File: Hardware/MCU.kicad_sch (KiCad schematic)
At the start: 32 parts, among them SW3 MCU_BOOT, SW4 reset, U14 STM32H743VITx, Y3 8MHz 12pF

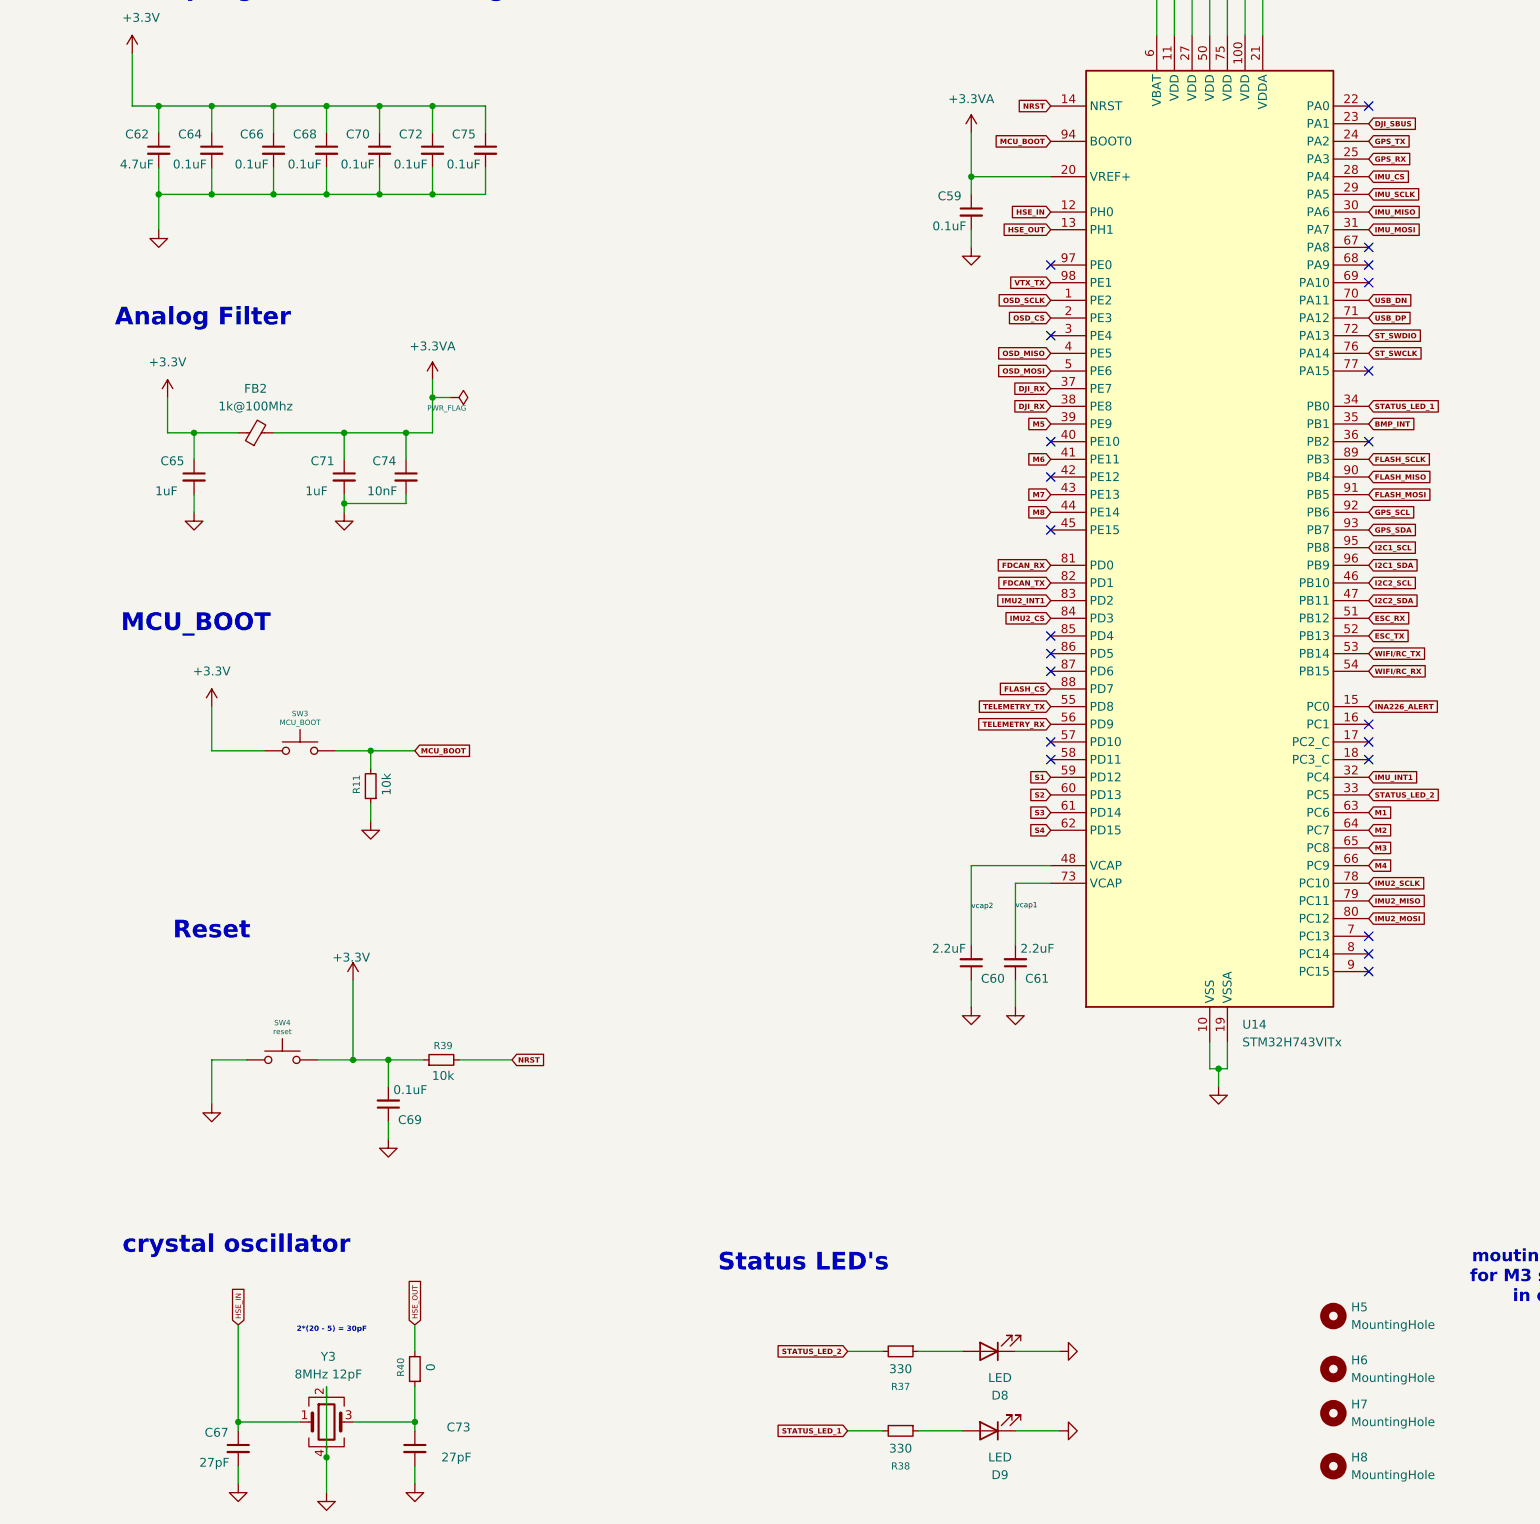
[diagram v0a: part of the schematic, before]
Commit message: Added Necessary Connectors, pads and comments in the respective file
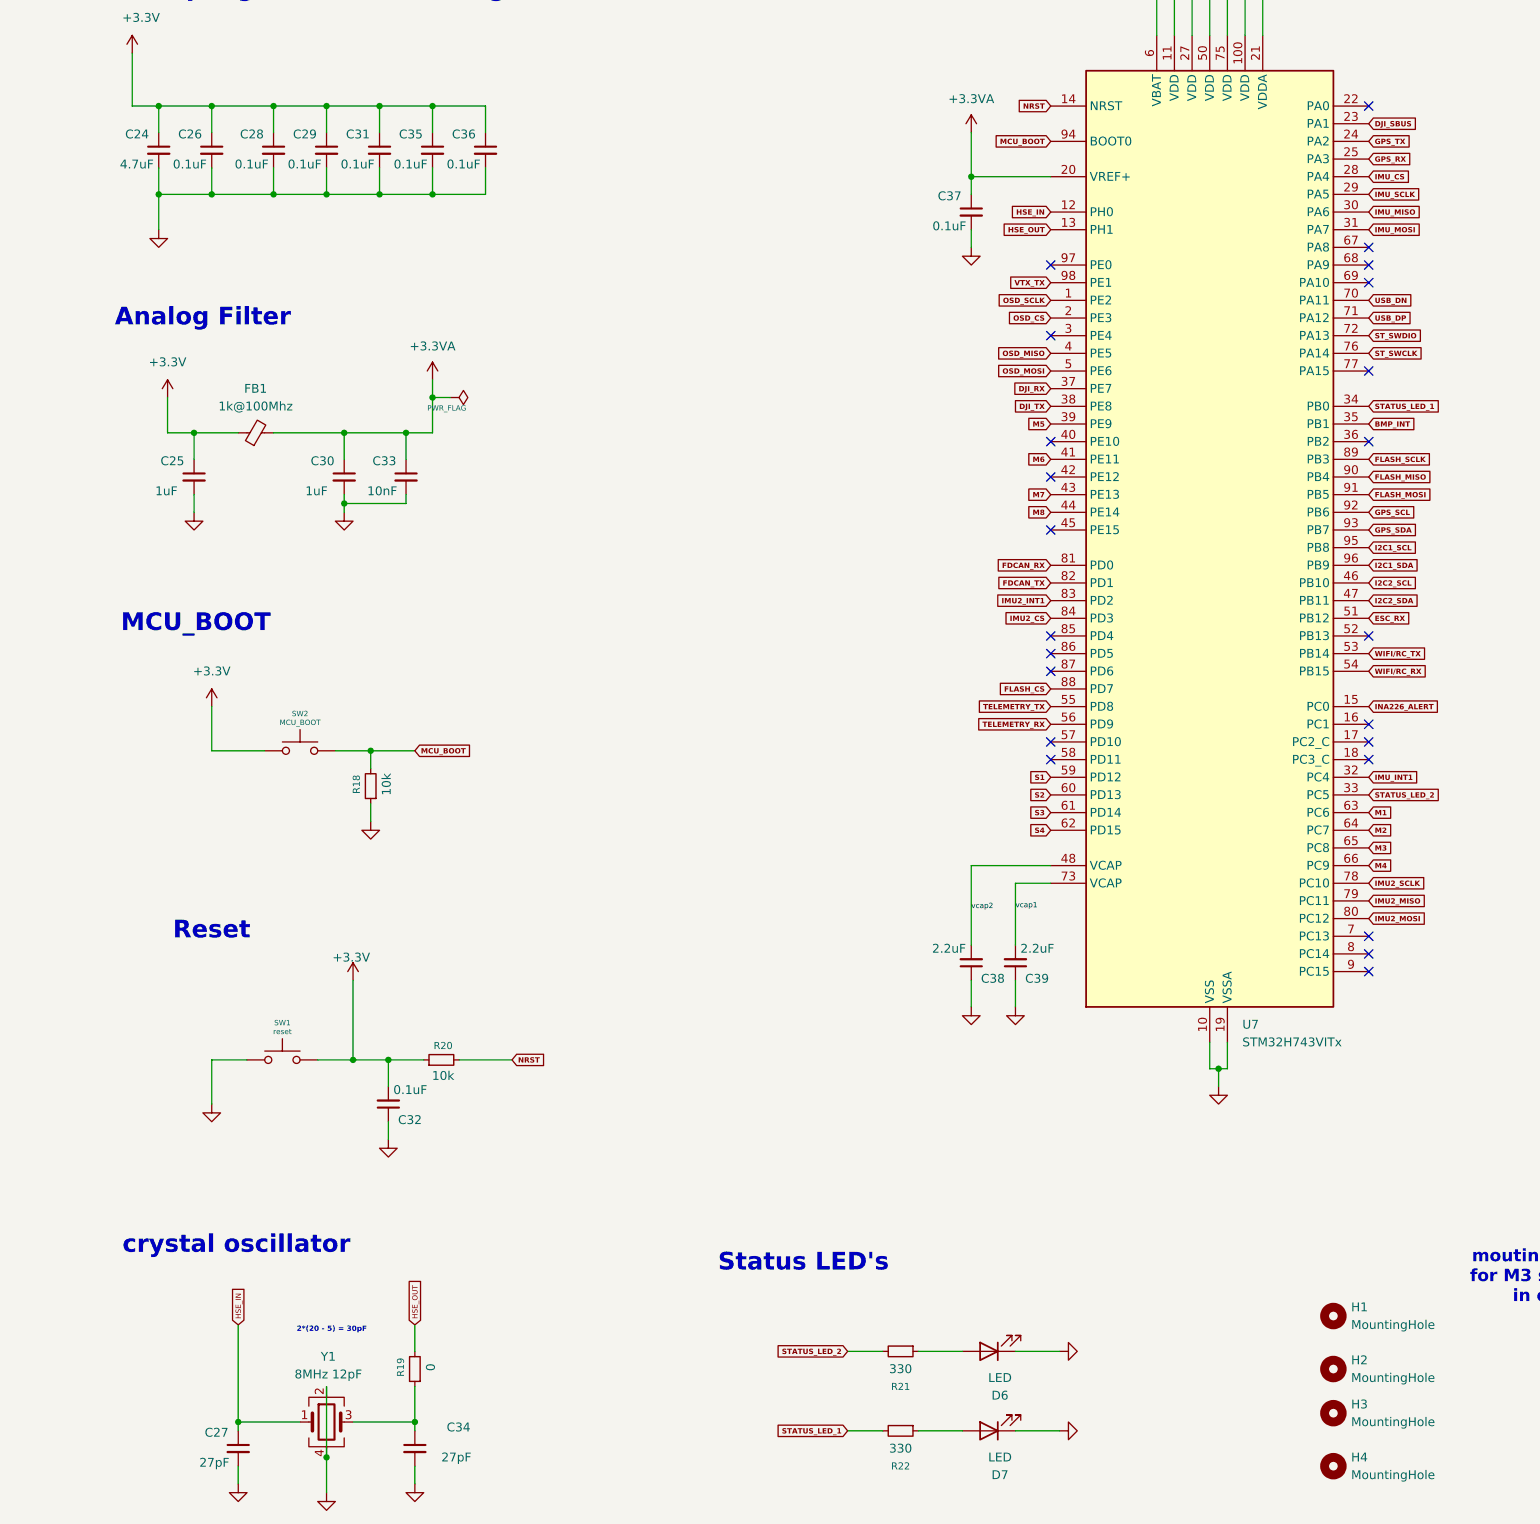
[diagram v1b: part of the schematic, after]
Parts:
- renumbered C62 to C24, C65 to C25, C64 to C26, C67 to C27, C66 to C28, C68 to C29, C71 to C30, C70 to C31, C69 to C32, C74 to C33, C73 to C34, C72 to C35, C75 to C36, C59 to C37, C60 to C38, C61 to C39, D8 to D6, D9 to D7, FB2 to FB1, H5 to H1, H6 to H2, H7 to H3, H8 to H4, R11 to R18, R40 to R19, R39 to R20, R37 to R21, R38 to R22, SW4 to SW1, SW3 to SW2, U14 to U7, Y3 to Y1
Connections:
- net DJI_RX: no longer U7.38 (PE8)
- net ESC_TX: no longer names the net of U7.52 (PB13)
- new net DJI_TX: U7.38 (PE8)
- no-connect marks 22 -> 23

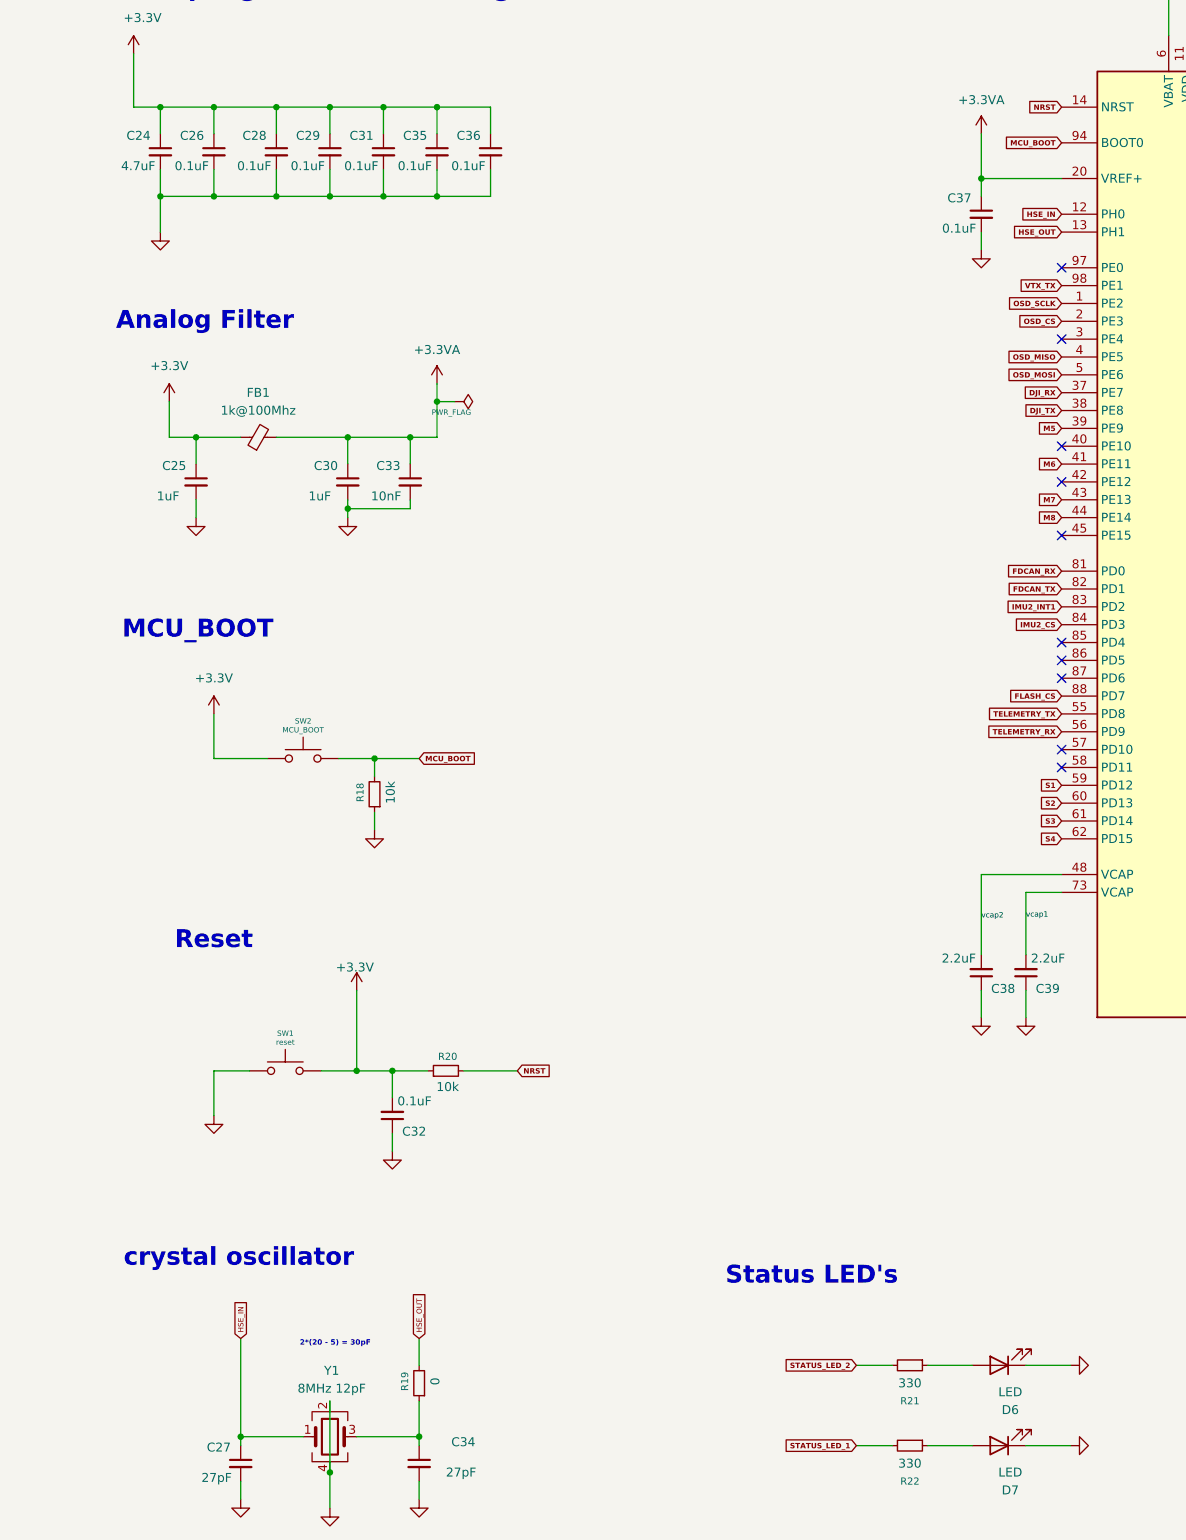
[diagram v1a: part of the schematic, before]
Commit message: Added Digital Airspeed Sensor Connector, Changed the Magnetometer
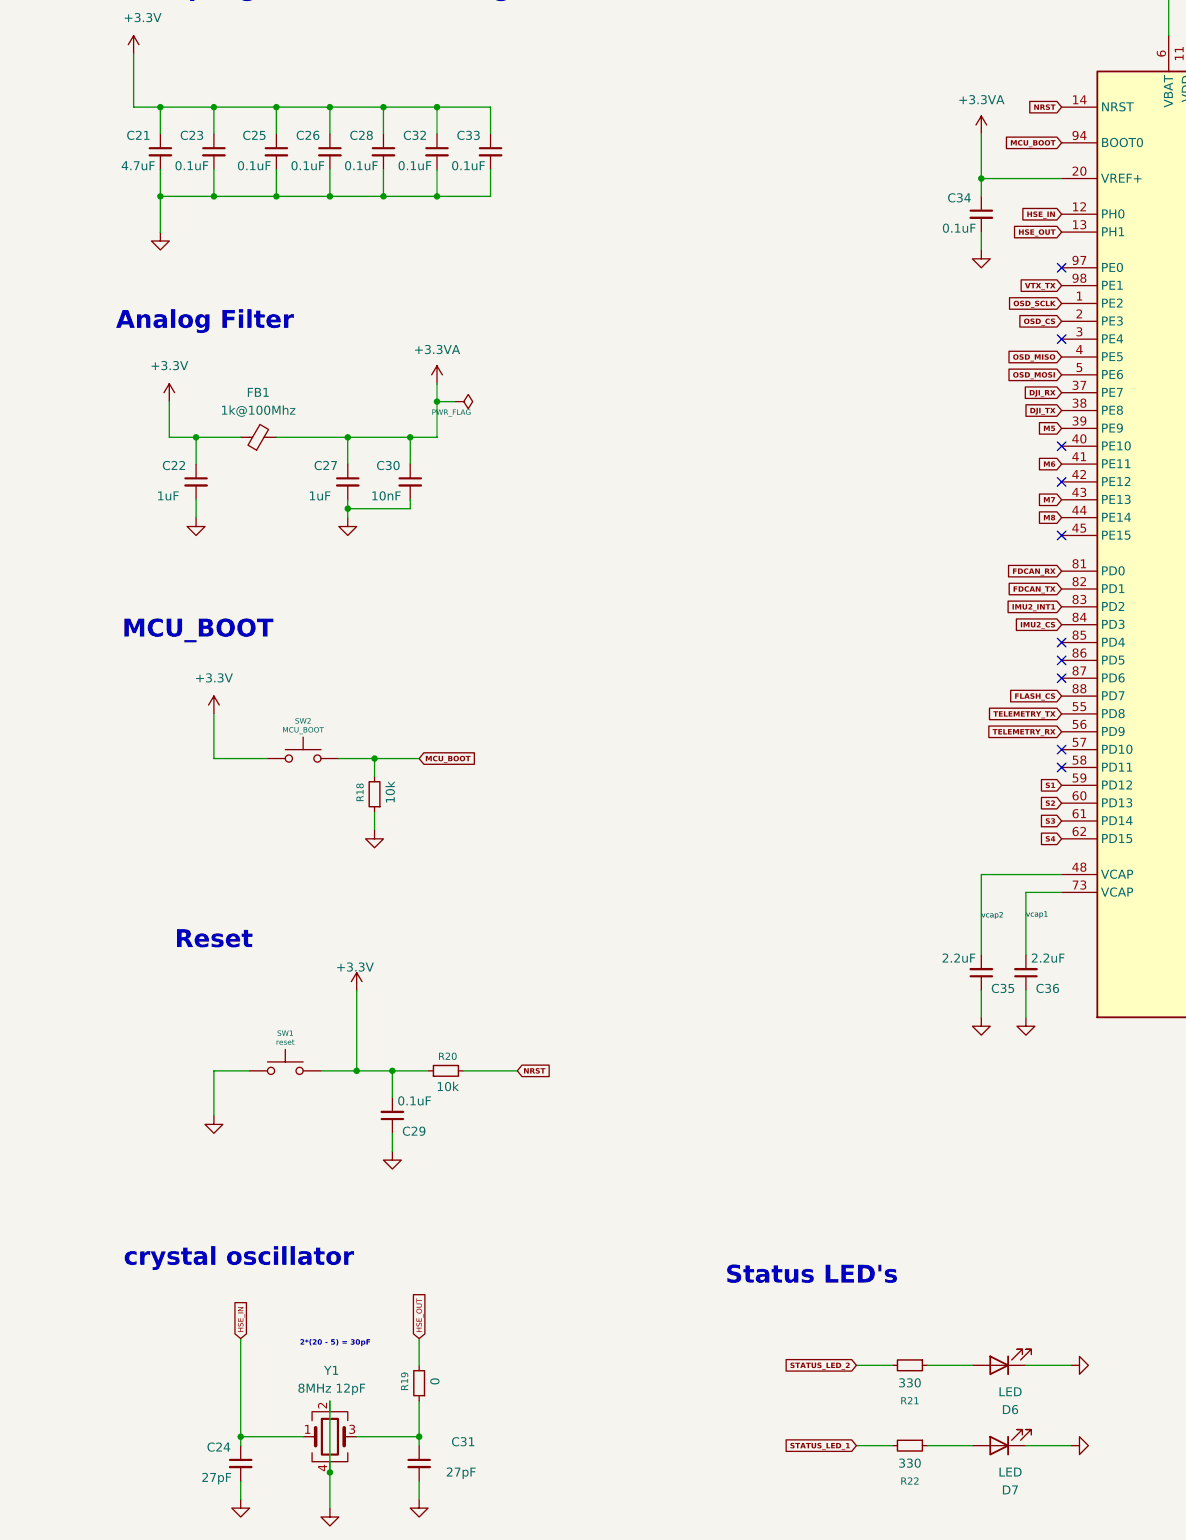
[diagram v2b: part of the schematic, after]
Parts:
- renumbered C24 to C21, C25 to C22, C26 to C23, C27 to C24, C28 to C25, C29 to C26, C30 to C27, C31 to C28, C32 to C29, C33 to C30, C34 to C31, C35 to C32, C36 to C33, C37 to C34, C38 to C35, C39 to C36

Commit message: Changed to CMOS, layout progress
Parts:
- removed C24, C31: 27pF, Capacitor_SMD:C_0402_1005Metric, symbol Device:C_Small
- removed R19: 0, Resistor_SMD:R_0402_1005Metric, symbol Device:R_Small
- removed Y1: 8MHz 12pF, Crystal:Crystal_SMD_3225-4Pin_3.2x2.5mm, symbol Device:Crystal_GND24
- added C21: 0.01uF, Capacitor_SMD:C_0603_1608Metric, symbol Device:C_Small
- added Y1: ASE-8.000MHZ-LC-T, Oscillator:Oscillator_SMD_Abracon_ASE-4Pin_3.2x2.5mm, symbol Oscillator:ASE-xxxMHz
- renumbered C21 to C22, C22 to C23, C23 to C24, C32 to C31, C33 to C32, C34 to C33, C35 to C34, C36 to C35, R18 to R15, R20 to R16, R21 to R17, R22 to R18
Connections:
- net +3.3V: now also C21.2, Y1.1 (EN), Y1.4 (Vdd)
- net GND: now also C21.1, Y1.2 (GND)
- net HSE_IN: now also Y1.3 (OUT)
- net HSE_OUT: no longer names the net of U7.13 (PH1)
- no-connect marks 23 -> 24
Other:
- note added: "1) Instead of using a crystal resonator for external clock source, We will use CMOS, BYPASS clock oscillator. Safer to get right and less hassle/requirements"
- note removed: "(Verification needed)"
- note removed: "1) Crystal Oscillator capacitor Calculation Depends on the specific crystal capacitance and stray capacitance. Take stray capacitance to be 3 - 5 pF."
- note removed: "2*(20 - 5) = 30pF"

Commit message: changed hella stuff in firmware plan and hardware pcb layout
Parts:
- added C56: 0.1uF, Capacitor_SMD:C_0402_1005Metric, symbol Device:C_Small
- added R6: 1k, Resistor_SMD:R_0402_1005Metric, symbol Device:R_Small
- added R7: 10k, Resistor_SMD:R_0402_1005Metric, symbol Device:R_Small
- C21: value 0.01uF -> 10nF
- D6, D7: footprint LED_SMD:LED_0402_1005Metric -> LED_SMD:LED_0805_2012Metric
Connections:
- net GND: now also C56.1
- net at U7.16 (PC1): now also R6.2, R7.1
- net CURR: now reaches U7.18 (PC3_C)
- net EXPANSION_TX: now reaches U7.52 (PB13)
- net ESC_RX renamed EXPANSION_RX
- net INA226_ALERT: no longer names the net of U7.15 (PC0)
- new net: C56.2, R6.1
- new net VBAT: R7.2
- no-connect marks 24 -> 22

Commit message: hella shit configured, layout progress
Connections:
- net EXPANSION_RX: now also U7.54 (PB15); no longer U7.51 (PB12)
- net EXPANSION_TX: now also U7.53 (PB14); no longer U7.52 (PB13)
- net FLASH_CS: now also U7.28 (PA4); no longer U7.88 (PD7)
- net FLASH_MISO: now also U7.30 (PA6); no longer U7.90 (PB4)
- net FLASH_MOSI: now also U7.31 (PA7); no longer U7.91 (PB5)
- net FLASH_SCLK: now also U7.29 (PA5); no longer U7.89 (PB3)
- net GPS_RX: now also U7.97 (PE0); no longer U7.25 (PA3)
- net GPS_TX: now also U7.98 (PE1); no longer U7.24 (PA2)
- net IMU2_CS: now also U7.88 (PD7); no longer U7.84 (PD3)
- net IMU2_INT1: now also U7.3 (PE4); no longer U7.83 (PD2)
- net IMU2_MISO: now also U7.90 (PB4); no longer U7.79 (PC11)
- net IMU2_MOSI: now also U7.91 (PB5); no longer U7.80 (PC12)
- net IMU2_SCLK: now also U7.89 (PB3); no longer U7.78 (PC10)
- net IMU_CS: now also U7.84 (PD3); no longer U7.28 (PA4)
- net IMU_INT1: now also U7.83 (PD2); no longer U7.32 (PC4)
- net IMU_MISO: now also U7.79 (PC11); no longer U7.30 (PA6)
- net IMU_MOSI: now also U7.80 (PC12); no longer U7.31 (PA7)
- net IMU_SCLK: now also U7.78 (PC10); no longer U7.29 (PA5)
- net OSD_CS: now also U7.7 (PC13); no longer U7.2 (PE3)
- net TELEMETRY_RX: now also U7.51 (PB12); no longer U7.56 (PD9)
- net TELEMETRY_TX: now also U7.52 (PB13); no longer U7.55 (PD8)
- net VTX_TX: now also U7.24 (PA2); no longer U7.98 (PE1)
- net WIFI/RC_RX: now also U7.56 (PD9); no longer U7.54 (PB15)
- net WIFI/RC_TX: now also U7.55 (PD8); no longer U7.53 (PB14)
- net VBAT renamed +VBAT

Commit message: added zener diode, more layout, Power verificatoin
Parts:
- C29: footprint Capacitor_SMD:C_0603_1608Metric -> Capacitor_SMD:C_0402_1005Metric
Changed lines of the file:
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@@
 			)
 		)
-		(property "Footprint" "Capacitor_SMD:C_0603_1608Metric"
+		(property "Footprint" "Capacitor_SMD:C_0402_1005Metric"
 			(at 73.66 196.85 0)
 			(effects
